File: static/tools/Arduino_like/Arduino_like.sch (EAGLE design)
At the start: 18 parts, among them IC1 MEGA8-P

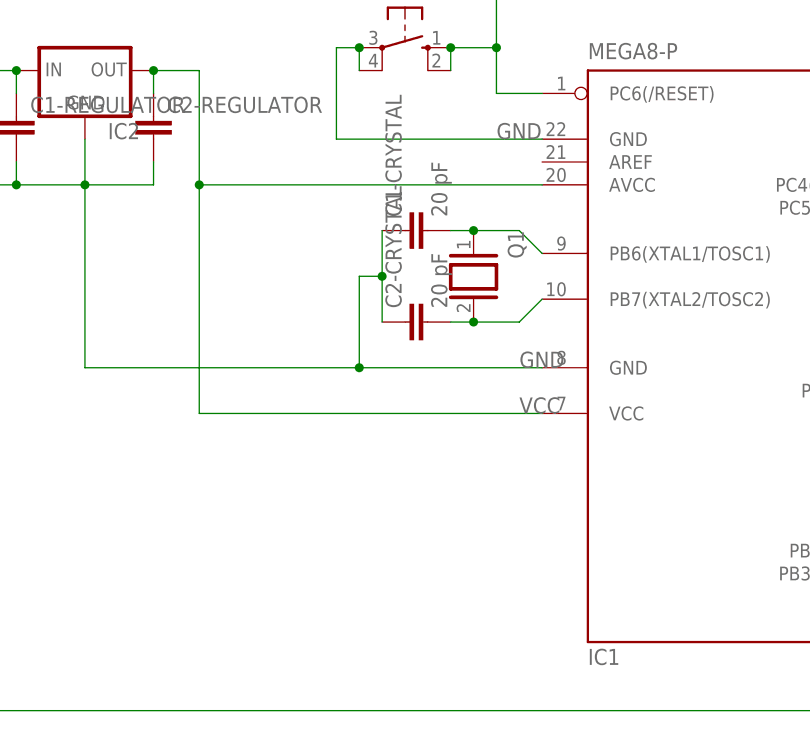
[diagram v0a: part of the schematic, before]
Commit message: [Arduino_like] adds GND, VCC and AREF pins.
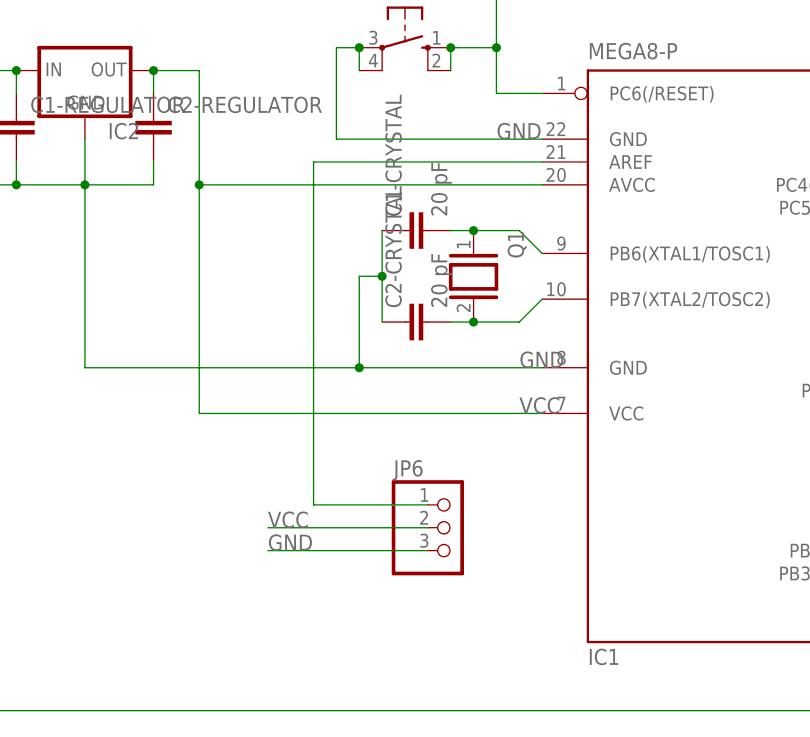
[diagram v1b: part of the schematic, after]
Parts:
- added JP6: (no value), pinhead:PINHD-1X3
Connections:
- new net N$29: IC1.AREF, JP6.1
- net GND: now also JP6.3
- net VCC: now also JP6.2
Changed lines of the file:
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@@
 <part name="JP3" library="pinhead" deviceset="PINHD-1X5" device=""/>
 <part name="JP5" library="pinhead" deviceset="PINHD-1X4" device=""/>
+<part name="JP6" library="pinhead" deviceset="PINHD-1X3" device=""/>
 </parts>
 <sheets>
@@
 <instance part="JP3" gate="A" x="160.02" y="38.1"/>
 <instance part="JP5" gate="A" x="182.88" y="50.8"/>
+<instance part="JP6" gate="A" x="83.82" y="43.18"/>
 </instances>
 <busses>
@@
 <pinref part="CAVALIER_VCC" gate="G$1" pin="2"/>
 <label x="228.6" y="43.18" size="1.778" layer="95"/>
+</segment>
+<segment>
+<pinref part="JP6" gate="A" pin="2"/>
+<wire x1="81.28" y1="43.18" x2="63.5" y2="43.18" width="0.1524" layer="91"/>
+<label x="63.5" y="43.18" size="1.778" layer="95"/>
 </segment>
 </net>
@@
 <label x="182.88" y="17.78" size="1.778" layer="95"/>
 </segment>
+<segment>
+<pinref part="JP6" gate="A" pin="3"/>
+<wire x1="81.28" y1="40.64" x2="63.5" y2="40.64" width="0.1524" layer="91"/>
+<label x="63.5" y="40.64" size="1.778" layer="95"/>
+</segment>
 </net>
 <net name="N$3" class="0">
@@
 </segment>
 </net>
+<net name="N$29" class="0">
+<segment>
+<pinref part="JP6" gate="A" pin="1"/>
+<wire x1="81.28" y1="45.72" x2="68.58" y2="45.72" width="0.1524" layer="91"/>
+<wire x1="68.58" y1="45.72" x2="68.58" y2="83.82" width="0.1524" layer="91"/>
+<wire x1="68.58" y1="83.82" x2="93.98" y2="83.82" width="0.1524" layer="91"/>
+<pinref part="IC1" gate="G$1" pin="AREF"/>
+</segment>
+</net>

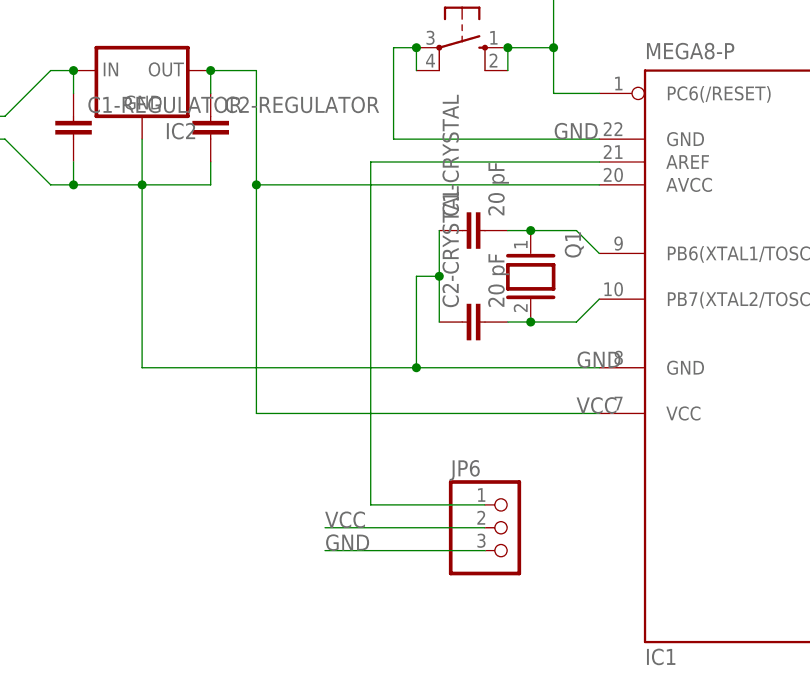
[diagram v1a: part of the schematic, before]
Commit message: [Arduino like] align pins.
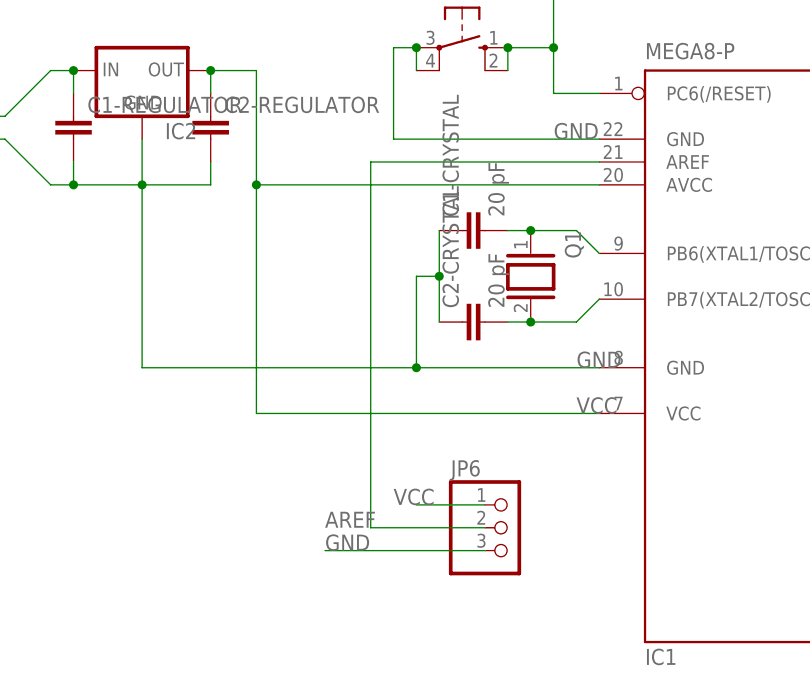
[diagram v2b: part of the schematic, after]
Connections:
- removed net N$29: IC1.AREF, JP6.1
- new net AREF: IC1.AREF, JP6.2
- net VCC: now also JP6.1; no longer JP6.2
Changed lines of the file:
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@@
 </segment>
 <segment>
-<pinref part="JP6" gate="A" pin="2"/>
-<wire x1="81.28" y1="43.18" x2="63.5" y2="43.18" width="0.1524" layer="91"/>
-<label x="63.5" y="43.18" size="1.778" layer="95"/>
+<pinref part="JP6" gate="A" pin="1"/>
+<wire x1="81.28" y1="45.72" x2="73.66" y2="45.72" width="0.1524" layer="91"/>
+<label x="71.12" y="45.72" size="1.778" layer="95"/>
 </segment>
 </net>
@@
 </segment>
 </net>
-<net name="N$29" class="0">
-<segment>
-<pinref part="JP6" gate="A" pin="1"/>
-<wire x1="81.28" y1="45.72" x2="68.58" y2="45.72" width="0.1524" layer="91"/>
-<wire x1="68.58" y1="45.72" x2="68.58" y2="83.82" width="0.1524" layer="91"/>
+<net name="AREF" class="0">
+<segment>
+<wire x1="68.58" y1="43.18" x2="68.58" y2="83.82" width="0.1524" layer="91"/>
 <wire x1="68.58" y1="83.82" x2="93.98" y2="83.82" width="0.1524" layer="91"/>
 <pinref part="IC1" gate="G$1" pin="AREF"/>
-</segment>
-</net>
+<pinref part="JP6" gate="A" pin="2"/>
+<wire x1="68.58" y1="43.18" x2="81.28" y2="43.18" width="0.1524" layer="91"/>
+<label x="63.5" y="43.18" size="1.778" layer="95"/>
+</segment>
+</net>

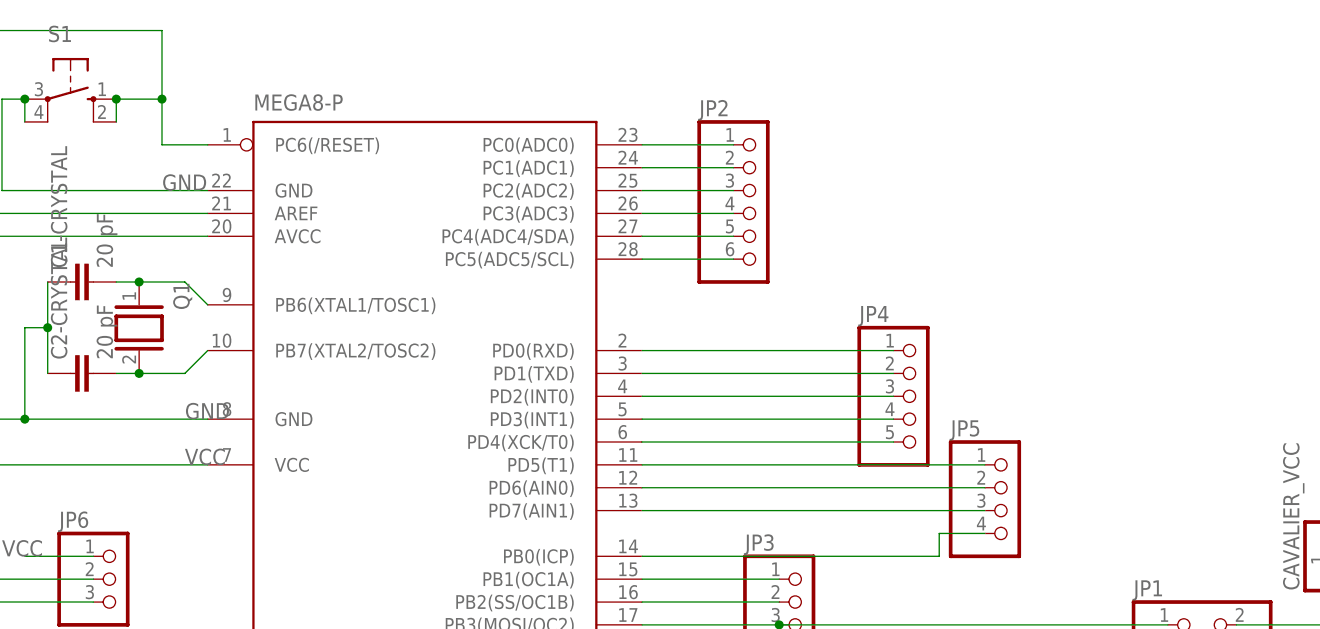
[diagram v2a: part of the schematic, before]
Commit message: [Arduino_like] add reset pin.
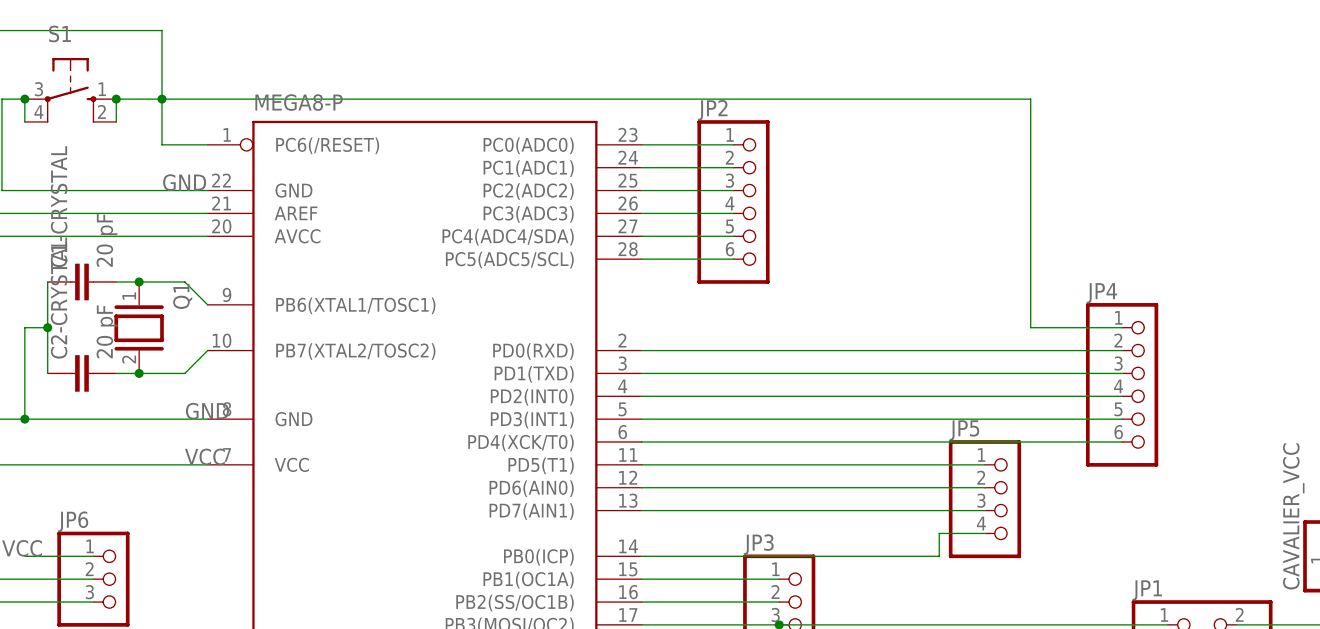
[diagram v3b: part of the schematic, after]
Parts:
- JP4: device pinhead:PINHD-1X5 -> pinhead:PINHD-1X6
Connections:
- net N$14: now also JP4.2; no longer JP4.1
- net N$16: now also JP4.3; no longer JP4.2
- net N$17: now also JP4.4; no longer JP4.3
- net N$18: now also JP4.5; no longer JP4.4
- net N$19: now also JP4.6; no longer JP4.5
- net N$4: now also JP4.1
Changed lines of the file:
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@@
 <grid distance="0.1" unitdist="inch" unit="inch" style="lines" multiple="1" display="no" altdistance="0.01" altunitdist="inch" altunit="inch"/>
 <layers>
-<layer number="1" name="Top" color="4" fill="1" visible="no" active="no"/>
-<layer number="2" name="Route2" color="1" fill="3" visible="no" active="no"/>
-<layer number="3" name="Route3" color="4" fill="3" visible="no" active="no"/>
-<layer number="4" name="Route4" color="1" fill="4" visible="no" active="no"/>
-<layer number="5" name="Route5" color="4" fill="4" visible="no" active="no"/>
-<layer number="6" name="Route6" color="1" fill="8" visible="no" active="no"/>
-<layer number="7" name="Route7" color="4" fill="8" visible="no" active="no"/>
-<layer number="8" name="Route8" color="1" fill="2" visible="no" active="no"/>
-<layer number="9" name="Route9" color="4" fill="2" visible="no" active="no"/>
-<layer number="10" name="Route10" color="1" fill="7" visible="no" active="no"/>
-<layer number="11" name="Route11" color="4" fill="7" visible="no" active="no"/>
-<layer number="12" name="Route12" color="1" fill="5" visible="no" active="no"/>
-<layer number="13" name="Route13" color="4" fill="5" visible="no" active="no"/>
-<layer number="14" name="Route14" color="1" fill="6" visible="no" active="no"/>
-<layer number="15" name="Route15" color="4" fill="6" visible="no" active="no"/>
-<layer number="16" name="Bottom" color="1" fill="1" visible="no" active="no"/>
-<layer number="17" name="Pads" color="2" fill="1" visible="no" active="no"/>
-<layer number="18" name="Vias" color="2" fill="1" visible="no" active="no"/>
-<layer number="19" name="Unrouted" color="6" fill="1" visible="no" active="no"/>
-<layer number="20" name="Dimension" color="15" fill="1" visible="no" active="no"/>
-<layer number="21" name="tPlace" color="7" fill="1" visible="no" active="no"/>
-<layer number="22" name="bPlace" color="7" fill="1" visible="no" active="no"/>
-<layer number="23" name="tOrigins" color="15" fill="1" visible="no" active="no"/>
-<layer number="24" name="bOrigins" color="15" fill="1" visible="no" active="no"/>
-<layer number="25" name="tNames" color="7" fill="1" visible="no" active="no"/>
-<layer number="26" name="bNames" color="7" fill="1" visible="no" active="no"/>
-<layer number="27" name="tValues" color="7" fill="1" visible="no" active="no"/>
-<layer number="28" name="bValues" color="7" fill="1" visible="no" active="no"/>
+<layer number="1" name="Top" color="4" fill="1" visible="yes" active="no"/>
+<layer number="2" name="Route2" color="1" fill="3" visible="yes" active="no"/>
+<layer number="3" name="Route3" color="4" fill="3" visible="yes" active="no"/>
+<layer number="4" name="Route4" color="1" fill="4" visible="yes" active="no"/>
+<layer number="5" name="Route5" color="4" fill="4" visible="yes" active="no"/>
+<layer number="6" name="Route6" color="1" fill="8" visible="yes" active="no"/>
+<layer number="7" name="Route7" color="4" fill="8" visible="yes" active="no"/>
+<layer number="8" name="Route8" color="1" fill="2" visible="yes" active="no"/>
+<layer number="9" name="Route9" color="4" fill="2" visible="yes" active="no"/>
+<layer number="10" name="Route10" color="1" fill="7" visible="yes" active="no"/>
+<layer number="11" name="Route11" color="4" fill="7" visible="yes" active="no"/>
+<layer number="12" name="Route12" color="1" fill="5" visible="yes" active="no"/>
+<layer number="13" name="Route13" color="4" fill="5" visible="yes" active="no"/>
+<layer number="14" name="Route14" color="1" fill="6" visible="yes" active="no"/>
+<layer number="15" name="Route15" color="4" fill="6" visible="yes" active="no"/>
+<layer number="16" name="Bottom" color="1" fill="1" visible="yes" active="no"/>
+<layer number="17" name="Pads" color="2" fill="1" visible="yes" active="no"/>
+<layer number="18" name="Vias" color="2" fill="1" visible="yes" active="no"/>
+<layer number="19" name="Unrouted" color="6" fill="1" visible="yes" active="no"/>
+<layer number="20" name="Dimension" color="15" fill="1" visible="yes" active="no"/>
+<layer number="21" name="tPlace" color="7" fill="1" visible="yes" active="no"/>
+<layer number="22" name="bPlace" color="7" fill="1" visible="yes" active="no"/>
+<layer number="23" name="tOrigins" color="15" fill="1" visible="yes" active="no"/>
+<layer number="24" name="bOrigins" color="15" fill="1" visible="yes" active="no"/>
+<layer number="25" name="tNames" color="7" fill="1" visible="yes" active="no"/>
+<layer number="26" name="bNames" color="7" fill="1" visible="yes" active="no"/>
+<layer number="27" name="tValues" color="7" fill="1" visible="yes" active="no"/>
+<layer number="28" name="bValues" color="7" fill="1" visible="yes" active="no"/>
 <layer number="29" name="tStop" color="7" fill="3" visible="no" active="no"/>
 <layer number="30" name="bStop" color="7" fill="6" visible="no" active="no"/>
@@
 <layer number="35" name="tGlue" color="7" fill="4" visible="no" active="no"/>
 <layer number="36" name="bGlue" color="7" fill="5" visible="no" active="no"/>
-<layer number="37" name="tTest" color="7" fill="1" visible="no" active="no"/>
-<layer number="38" name="bTest" color="7" fill="1" visible="no" active="no"/>
+<layer number="37" name="tTest" color="7" fill="1" visible="yes" active="no"/>
+<layer number="38" name="bTest" color="7" fill="1" visible="yes" active="no"/>
 <layer number="39" name="tKeepout" color="4" fill="11" visible="no" active="no"/>
 <layer number="40" name="bKeepout" color="1" fill="11" visible="no" active="no"/>
@@
 <layer number="44" name="Drills" color="7" fill="1" visible="no" active="no"/>
 <layer number="45" name="Holes" color="7" fill="1" visible="no" active="no"/>
-<layer number="46" name="Milling" color="3" fill="1" visible="no" active="no"/>
-<layer number="47" name="Measures" color="7" fill="1" visible="no" active="no"/>
-<layer number="48" name="Document" color="7" fill="1" visible="no" active="no"/>
-<layer number="49" name="Reference" color="7" fill="1" visible="no" active="no"/>
-<layer number="51" name="tDocu" color="7" fill="1" visible="no" active="no"/>
-<layer number="52" name="bDocu" color="7" fill="1" visible="no" active="no"/>
+<layer number="46" name="Milling" color="3" fill="1" visible="yes" active="no"/>
+<layer number="47" name="Measures" color="7" fill="1" visible="yes" active="no"/>
+<layer number="48" name="Document" color="7" fill="1" visible="yes" active="no"/>
+<layer number="49" name="Reference" color="7" fill="1" visible="yes" active="no"/>
+<layer number="51" name="tDocu" color="7" fill="1" visible="yes" active="no"/>
+<layer number="52" name="bDocu" color="7" fill="1" visible="yes" active="no"/>
 <layer number="91" name="Nets" color="2" fill="1" visible="yes" active="yes"/>
 <layer number="92" name="Busses" color="1" fill="1" visible="yes" active="yes"/>
@@
 <part name="LED1" library="led" deviceset="LED" device="3MM"/>
 <part name="S1" library="switch-omron" deviceset="10-XX" device=""/>
-<part name="JP4" library="pinhead" deviceset="PINHD-1X5" device=""/>
 <part name="JP3" library="pinhead" deviceset="PINHD-1X5" device=""/>
 <part name="JP5" library="pinhead" deviceset="PINHD-1X4" device=""/>
 <part name="JP6" library="pinhead" deviceset="PINHD-1X3" device=""/>
+<part name="JP4" library="pinhead" deviceset="PINHD-1X6" device=""/>
 </parts>
 <sheets>
@@
 <instance part="LED1" gate="G$1" x="172.72" y="17.78" rot="R90"/>
 <instance part="S1" gate="1" x="78.74" y="96.52" rot="R270"/>
-<instance part="JP4" gate="A" x="172.72" y="63.5"/>
 <instance part="JP3" gate="A" x="160.02" y="38.1"/>
 <instance part="JP5" gate="A" x="182.88" y="50.8"/>
 <instance part="JP6" gate="A" x="83.82" y="43.18"/>
+<instance part="JP4" gate="A" x="198.12" y="63.5"/>
 </instances>
 <busses>
@@
 <wire x1="83.82" y1="93.98" x2="83.82" y2="96.52" width="0.1524" layer="91"/>
 <junction x="83.82" y="96.52"/>
+<pinref part="JP4" gate="A" pin="1"/>
+<wire x1="195.58" y1="71.12" x2="185.42" y2="71.12" width="0.1524" layer="91"/>
+<wire x1="185.42" y1="71.12" x2="185.42" y2="96.52" width="0.1524" layer="91"/>
+<wire x1="185.42" y1="96.52" x2="88.9" y2="96.52" width="0.1524" layer="91"/>
 </segment>
 </net>
@@
 <segment>
 <pinref part="IC1" gate="G$1" pin="PD0(RXD)"/>
-<wire x1="142.24" y1="68.58" x2="170.18" y2="68.58" width="0.1524" layer="91"/>
-<pinref part="JP4" gate="A" pin="1"/>
+<wire x1="142.24" y1="68.58" x2="195.58" y2="68.58" width="0.1524" layer="91"/>
+<pinref part="JP4" gate="A" pin="2"/>
 </segment>
 </net>
@@
 <segment>
 <pinref part="IC1" gate="G$1" pin="PD1(TXD)"/>
-<wire x1="170.18" y1="66.04" x2="142.24" y2="66.04" width="0.1524" layer="91"/>
-<pinref part="JP4" gate="A" pin="2"/>
+<wire x1="195.58" y1="66.04" x2="142.24" y2="66.04" width="0.1524" layer="91"/>
+<pinref part="JP4" gate="A" pin="3"/>
 </segment>
 </net>
@@
 <segment>
 <pinref part="IC1" gate="G$1" pin="PD2(INT0)"/>
-<wire x1="142.24" y1="63.5" x2="170.18" y2="63.5" width="0.1524" layer="91"/>
-<pinref part="JP4" gate="A" pin="3"/>
+<wire x1="142.24" y1="63.5" x2="195.58" y2="63.5" width="0.1524" layer="91"/>
+<pinref part="JP4" gate="A" pin="4"/>
 </segment>
 </net>
@@
 <segment>
 <pinref part="IC1" gate="G$1" pin="PD3(INT1)"/>
-<wire x1="170.18" y1="60.96" x2="142.24" y2="60.96" width="0.1524" layer="91"/>
-<pinref part="JP4" gate="A" pin="4"/>
+<wire x1="195.58" y1="60.96" x2="142.24" y2="60.96" width="0.1524" layer="91"/>
+<pinref part="JP4" gate="A" pin="5"/>
 </segment>
 </net>
@@
 <segment>
 <pinref part="IC1" gate="G$1" pin="PD4(XCK/T0)"/>
-<wire x1="170.18" y1="58.42" x2="142.24" y2="58.42" width="0.1524" layer="91"/>
-<pinref part="JP4" gate="A" pin="5"/>
-</segment>
-</net>
+<wire x1="195.58" y1="58.42" x2="142.24" y2="58.42" width="0.1524" layer="91"/>
+<pinref part="JP4" gate="A" pin="6"/>
+</segment>
+</net>
